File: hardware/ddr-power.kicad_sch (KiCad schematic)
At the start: 6 parts

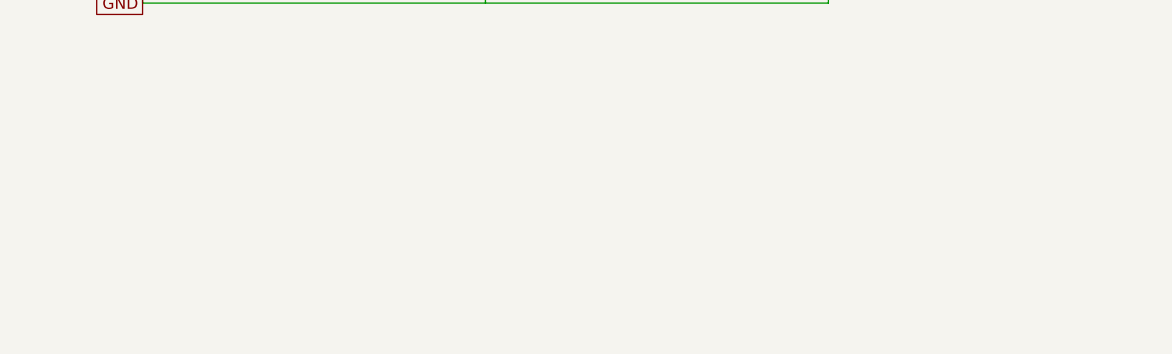
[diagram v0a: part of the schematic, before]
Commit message: Capture processor DDR RZQ pull-up and unused VREF output
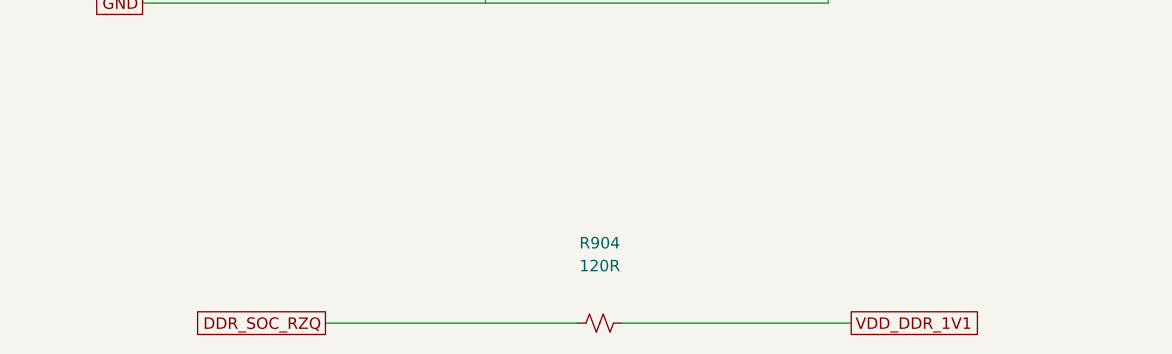
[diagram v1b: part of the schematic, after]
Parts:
- added R904: 120R, Resistor_SMD:R_0603_1608Metric, symbol Device:R_Small_US
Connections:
- net VDD_DDR_1V1: now also R904.2
- new net DDR_SOC_RZQ: R904.1

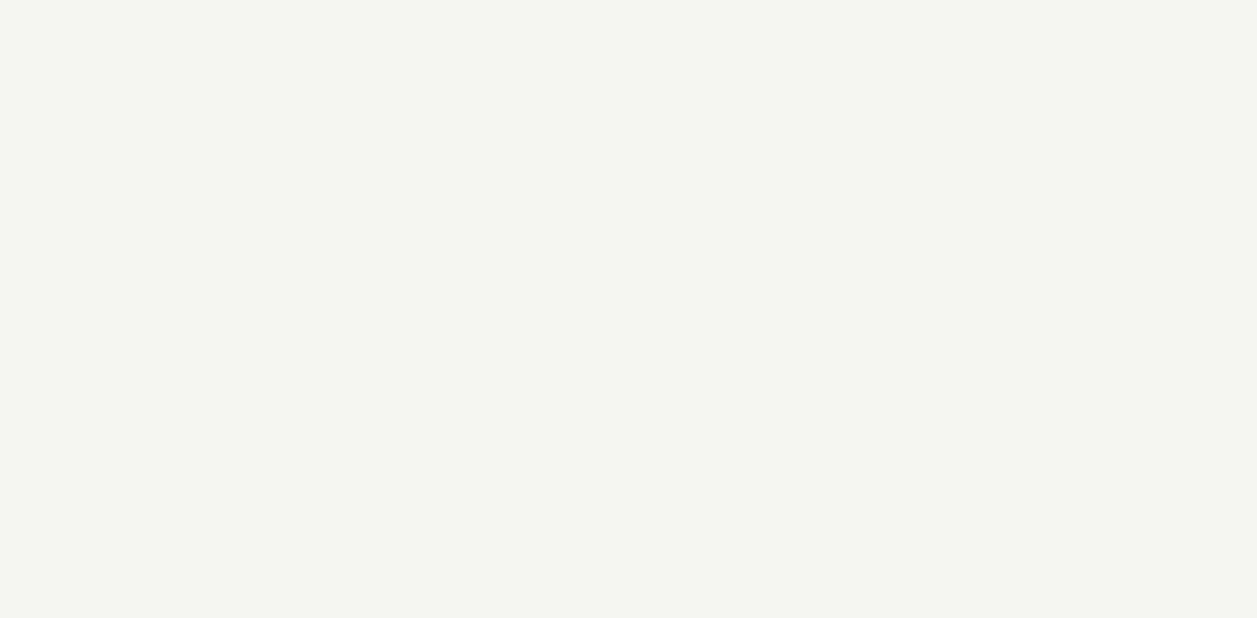
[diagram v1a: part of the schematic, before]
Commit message: Capture audited VDDQ regulator and local input bypass draft
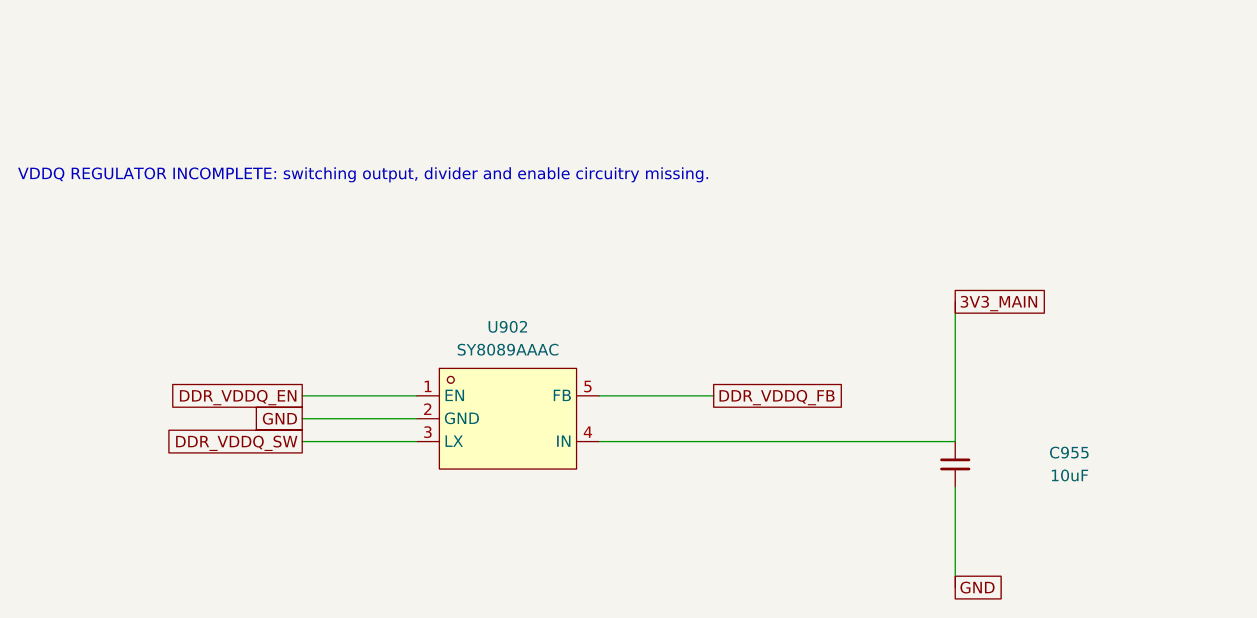
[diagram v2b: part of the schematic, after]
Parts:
- added C955: 10uF, Capacitor_SMD:C_1206_3216Metric, symbol Device:C_Small
- added U902: SY8089AAAC, symbol DdrPowerDraft:SY8089AAAC
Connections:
- net GND: now also C955.2, U902.2 (GND)
- new net 3V3_MAIN: C955.1, U902.4 (IN)
- new net DDR_VDDQ_EN: U902.1 (EN)
- new net DDR_VDDQ_FB: U902.5 (FB)
- new net DDR_VDDQ_SW: U902.3 (LX)
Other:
- note added: "VDDQ REGULATOR INCOMPLETE: switching output, divider and enable circuitry missing."

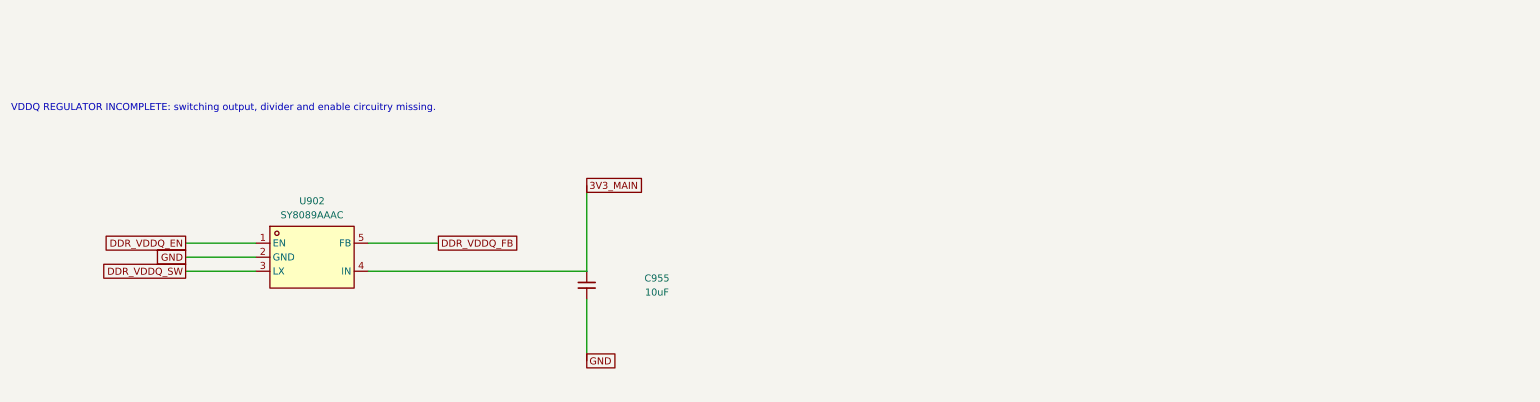
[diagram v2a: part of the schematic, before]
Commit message: Capture VDDQ enable RC and default-off discharge resistor
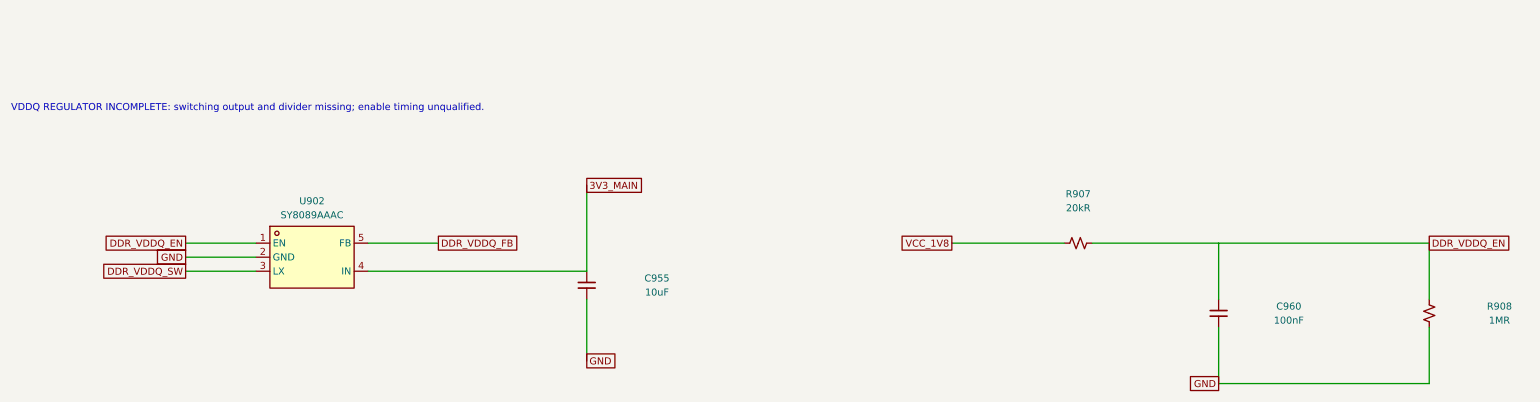
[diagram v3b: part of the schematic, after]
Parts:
- added C960: 100nF, Capacitor_SMD:C_0603_1608Metric, symbol Device:C_Small
- added R907: 20kR, Resistor_SMD:R_0603_1608Metric, symbol Device:R_Small_US
- added R908: 1MR, Resistor_SMD:R_0603_1608Metric, symbol Device:R_Small_US
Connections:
- net DDR_VDDQ_EN: now also R907.2, R908.1
- net GND: now also C960.2, R908.2
- new net VCC_1V8: R907.1
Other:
- note added: "VDDQ REGULATOR INCOMPLETE: switching output and divider missing; enable timing unqualified."
- note removed: "VDDQ REGULATOR INCOMPLETE: switching output, divider and enable circuitry missing."

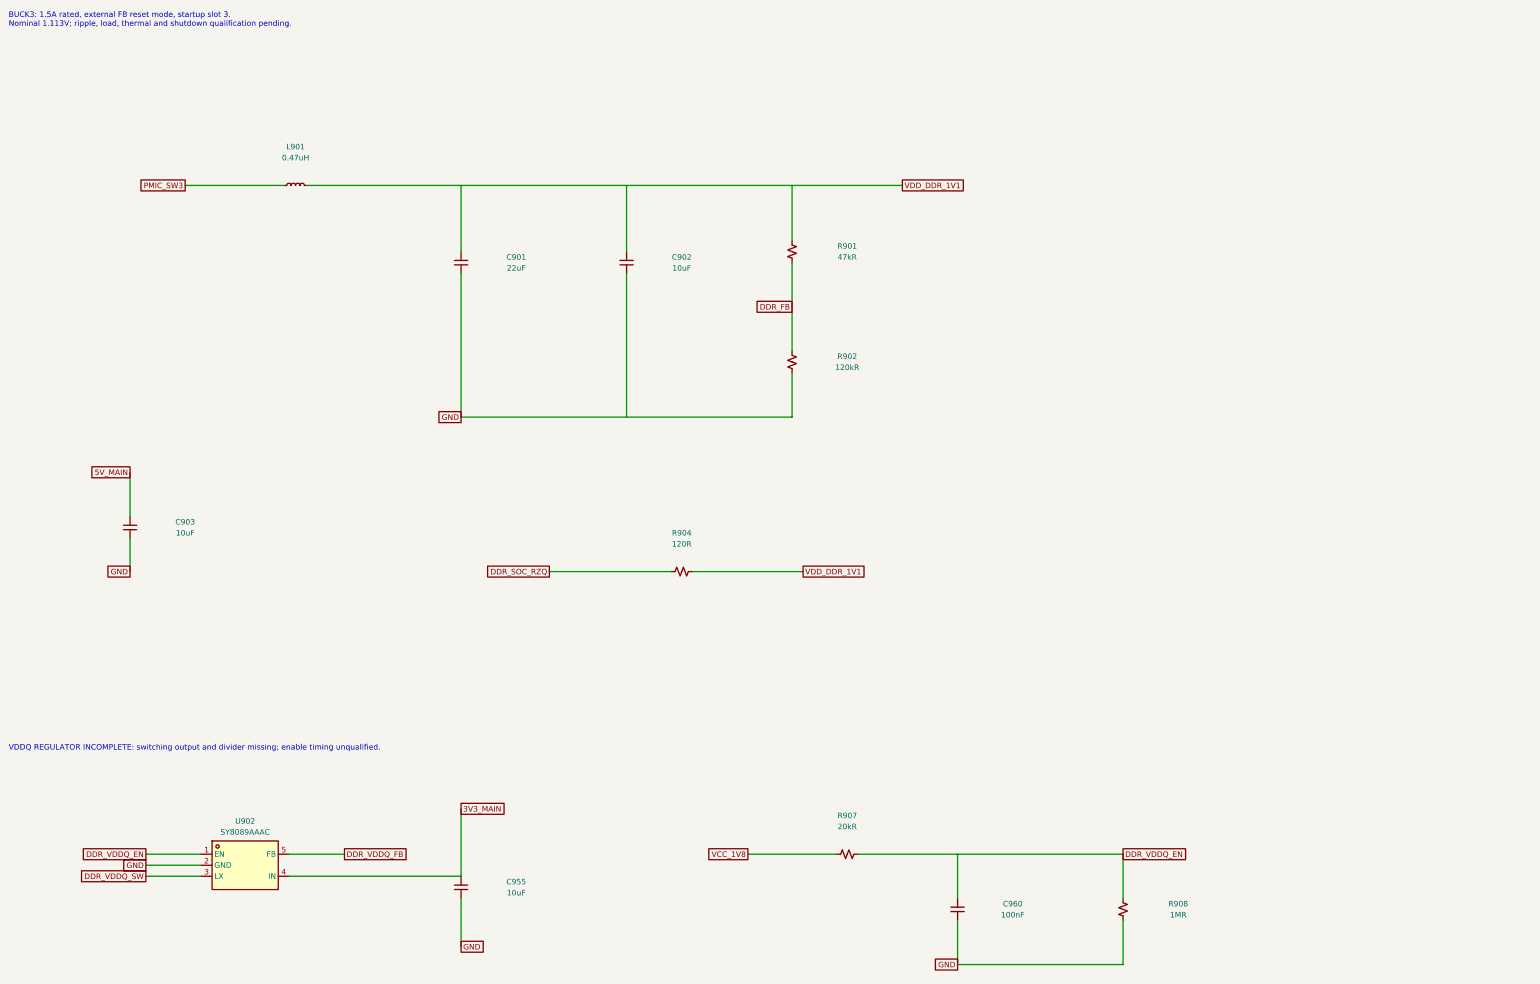
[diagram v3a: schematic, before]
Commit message: Capture VDDQ feedback divider and C0G feed-forward capacitor
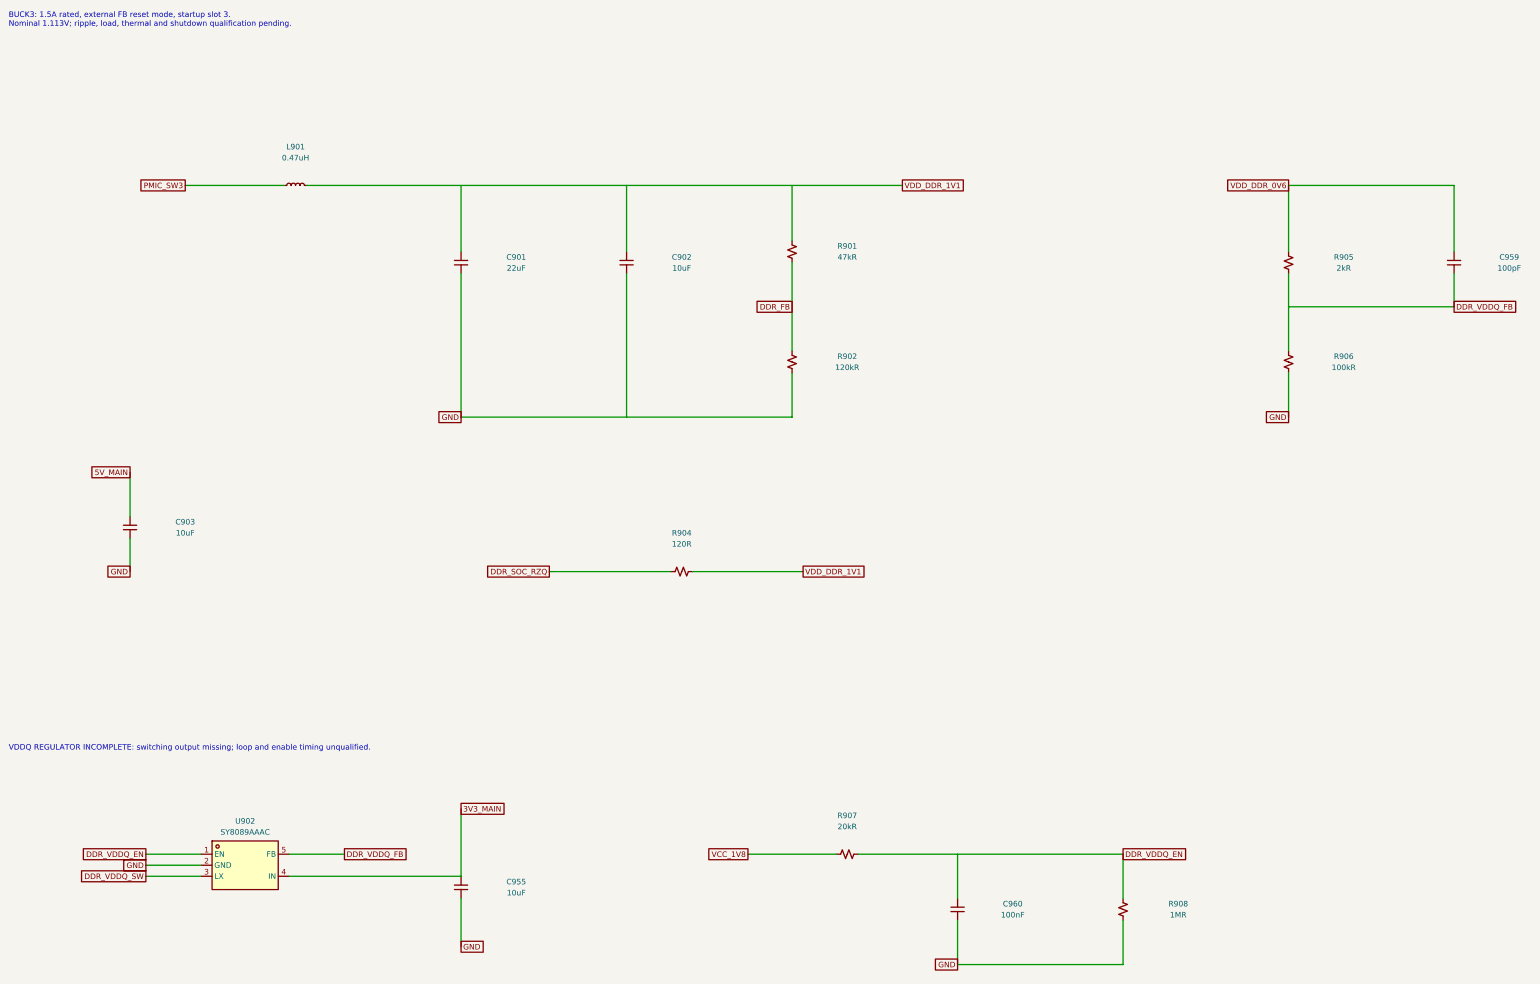
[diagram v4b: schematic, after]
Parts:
- added C959: 100pF, Capacitor_SMD:C_0603_1608Metric, symbol Device:C_Small
- added R905: 2kR, Resistor_SMD:R_0603_1608Metric, symbol Device:R_Small_US
- added R906: 100kR, Resistor_SMD:R_0603_1608Metric, symbol Device:R_Small_US
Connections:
- net DDR_VDDQ_FB: now also C959.2, R905.2, R906.1
- net GND: now also R906.2
- new net VDD_DDR_0V6: C959.1, R905.1
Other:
- note added: "VDDQ REGULATOR INCOMPLETE: switching output missing; loop and enable timing unqualified."
- note removed: "VDDQ REGULATOR INCOMPLETE: switching output and divider missing; enable timing unqualified."

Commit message: Complete appliance engineering schematic capture
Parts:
- added C956, C957: 22uF, Capacitor_SMD:C_1210_3225Metric, symbol Device:C_Small
- added C958: 10uF, Capacitor_SMD:C_1206_3216Metric, symbol Device:C_Small
- added L902: 2.2uH, Inductor_SMD:L_Coilcraft_XxL4020, symbol Device:L_Small
- C955: Qualification U902 input bypass; effective capacitance and layout pending -> U902 input bypass; place at IN/GND
- U902: footprint (none) -> Package_TO_SOT_SMD:SOT-23-5; Qualification DRAFT: VDDQ regulator output, feedback, enable and footprin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 -> Reference LPDDR4X supply; load, loop and sequencing require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
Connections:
- net DDR_VDDQ_SW: now also L902.1
- net GND: now also C956.2, C958.2
- net VDD_DDR_0V6: now also C958.1, L902.2
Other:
- note added: "LPDDR4X 0.612V nominal: 2.2uH, 22uF + 22uF + 10uF output. Place FB sense at load; verify load, ripple, loop and rail order on hardware."
- note removed: "VDDQ REGULATOR INCOMPLETE: switching output missing; loop and enable timing unqualified."
- title: DDR BUCK3 supply — DRAFT -> DDR and VDDQ supplies — engineering capture
- moved on the sheet: C955, C960, R907, R908, U902
